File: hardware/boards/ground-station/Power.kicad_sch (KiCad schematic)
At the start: 25 parts, among them J2 Barrel_Jack, U3 TPS564242DRLR, U4 TPS564242DRLR

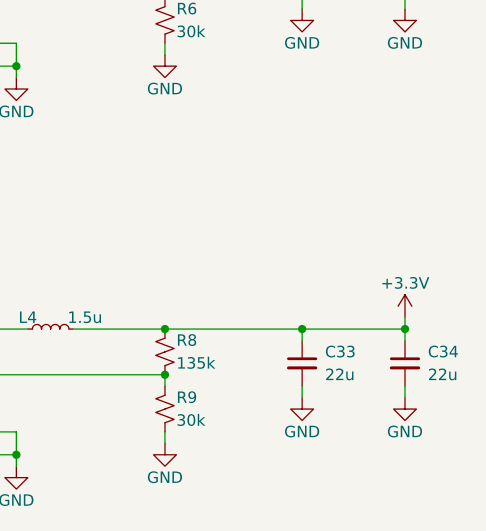
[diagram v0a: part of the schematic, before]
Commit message: Transmitting power (without wires) (wire delete)
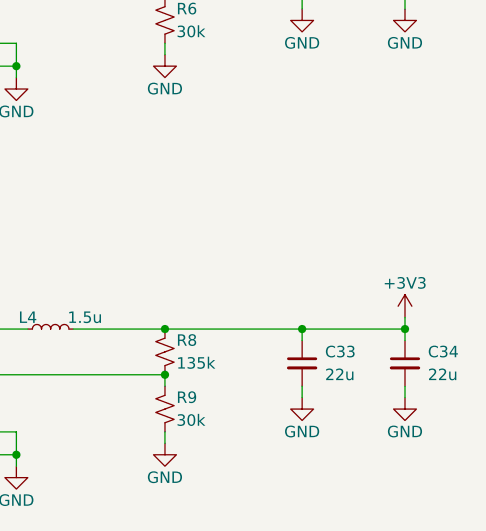
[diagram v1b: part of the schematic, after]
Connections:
- net +3.3V renamed +3V3
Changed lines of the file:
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@@
+    )
+  )
+  (symbol (lib_id "power:+3V3") (at 220.98 81.28 0) (unit 1)
+    (in_bom yes) (on_board yes) (dnp no)
+    (property "Reference" "#PWR0604" (at 220.98 85.09 0)
+      (effects (font (size 1.27 1.27)) hide)
+    )
+    (property "Value" "+3V3" (at 220.98 77.47 0)
+      (effects (font (size 1.27 1.27)))
+    )
+    (property "Footprint" "" (at 220.98 81.28 0)
+      (effects (font (size 1.27 1.27)) hide)
+    )
+    (property "Datasheet" "" (at 220.98 81.28 0)
+      (effects (font (size 1.27 1.27)) hide)
+    )
+    (pin "1")
+    (instances
+      (project "ground-station"
+        (path "/ce329892-de08-4d39-b253-15f3aaf1c085/448ef7a9-bc5a-4b03-856d-4da8b62bdbd1"
+          (reference "#PWR0604") (unit 1)
+        )
+      )
     )
   )
@@
         )
       )
-    )
-  )
-  (symbol (lib_id "power:+3.3V") (at 220.98 81.28 0) (unit 1)
-    (in_bom yes) (on_board yes) (dnp no)
-    (property "Reference" "#PWR030" (at 220.98 85.09 0)
-      (effects (font (size 1.27 1.27)) hide)
-    )
-    (property "Value" "+3.3V" (at 220.98 77.47 0)
-      (effects (font (size 1.27 1.27)))
-    )
-    (property "Footprint" "" (at 220.98 81.28 0)
-      (effects (font (size 1.27 1.27)) hide)
-    )
-    (property "Datasheet" "" (at 220.98 81.28 0)
-      (effects (font (size 1.27 1.27)) hide)
-    )
-    (pin "1")
-    (instances
-      (project "ground-station"
-        (path "/ce329892-de08-4d39-b253-15f3aaf1c085/448ef7a9-bc5a-4b03-856d-4da8b62bdbd1"
-          (reference "#PWR030") (unit 1)
-        )
-      )

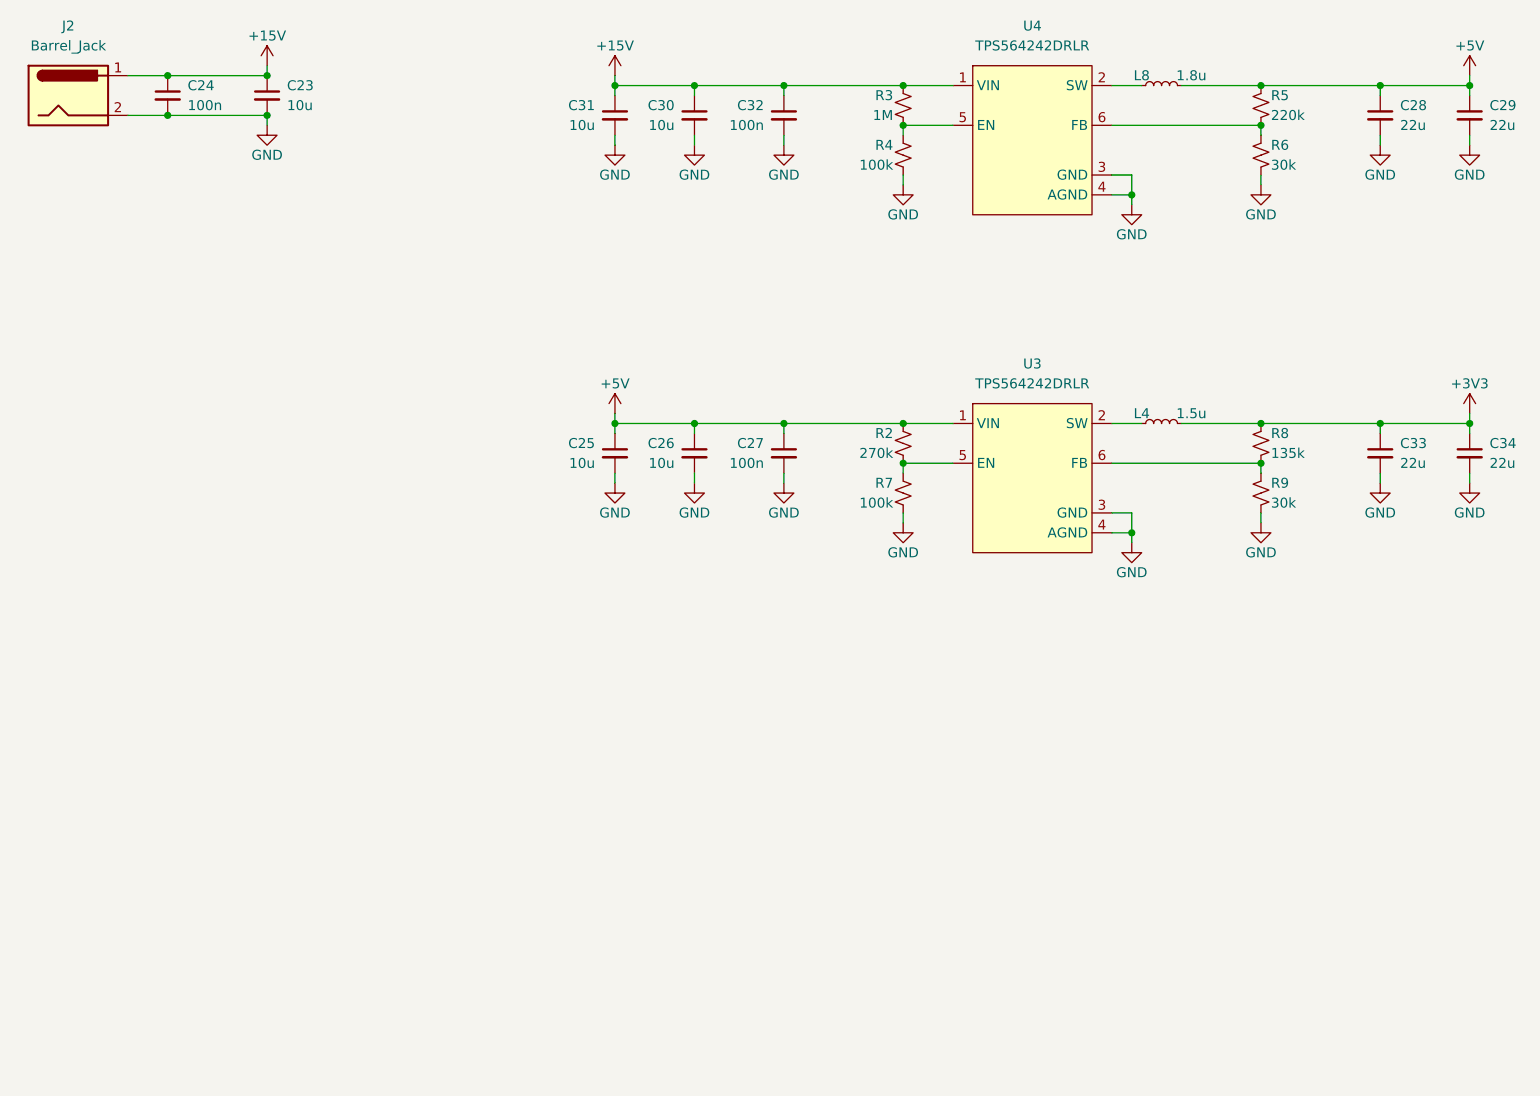
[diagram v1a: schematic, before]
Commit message: Change board input power to 5V, add connector for OTS wireless power TX
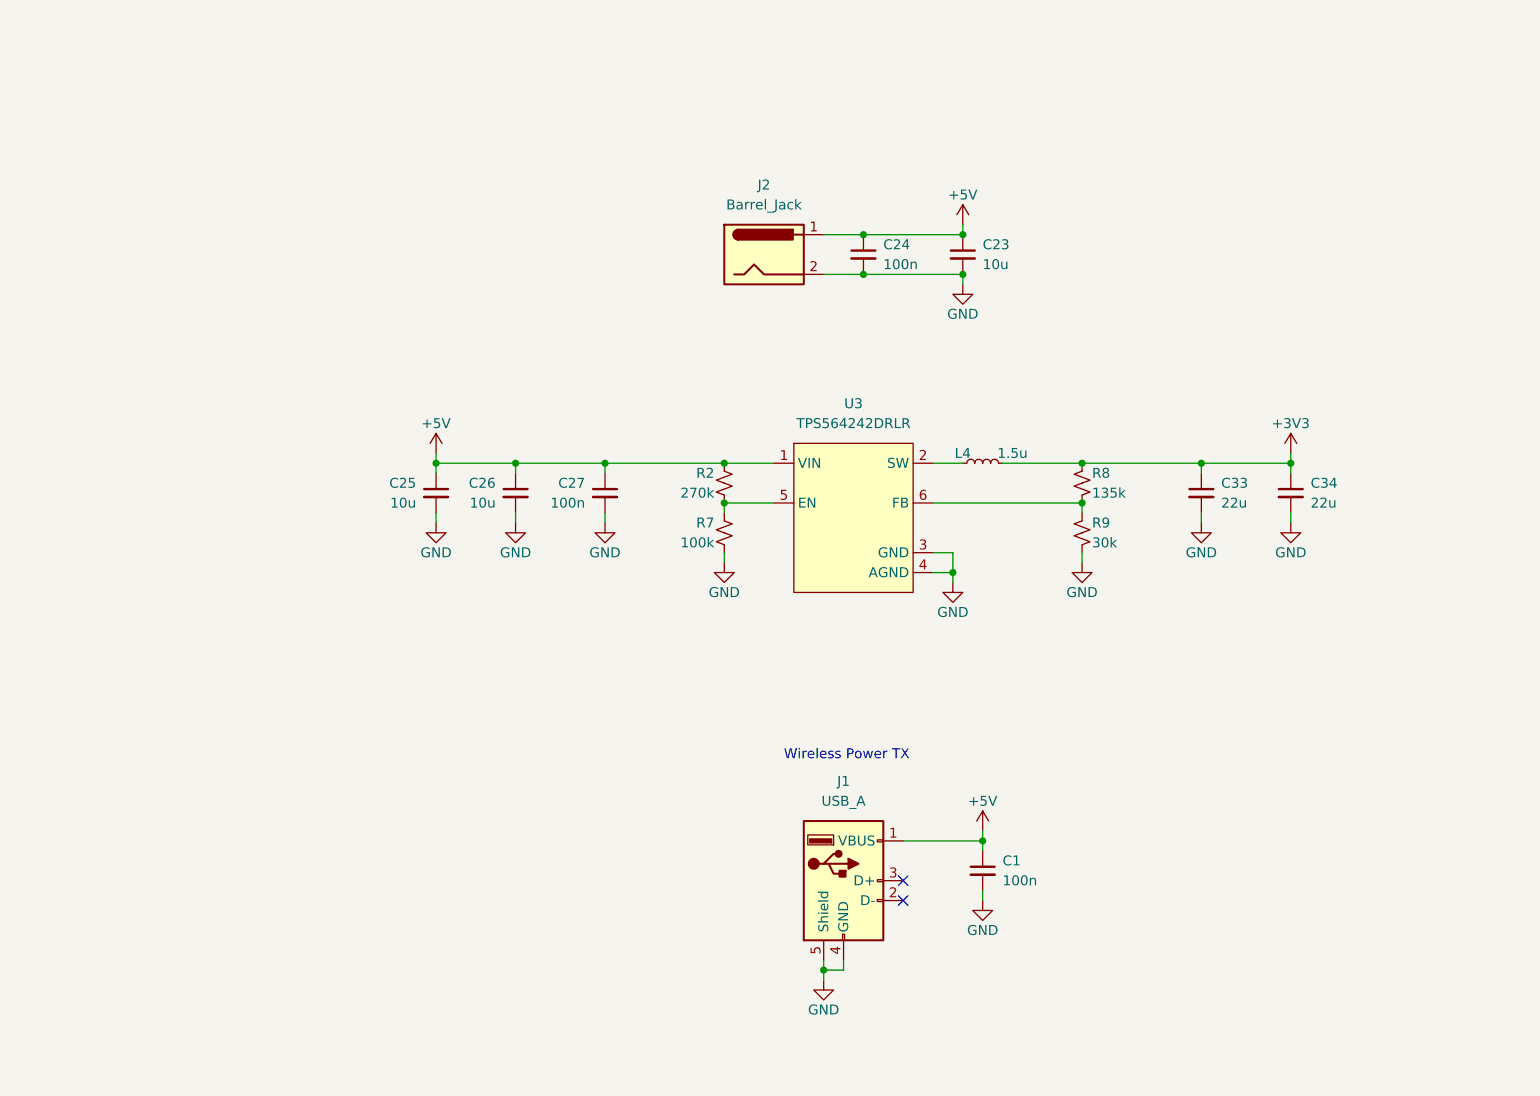
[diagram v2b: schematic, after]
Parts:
- removed C28, C29: 22u, symbol Device:C_Small
- removed C30, C31: 10u, symbol Device:C_Small
- removed C32: 100n, symbol Device:C_Small
- removed L8: 1.8u, symbol Device:L_Small
- removed R3: 1M, symbol Device:R_Small_US
- removed R4: 100k, symbol Device:R_Small_US
- removed R5: 220k, symbol Device:R_Small_US
- removed R6: 30k, symbol Device:R_Small_US
- removed U4: TPS564242DRLR, Package_TO_SOT_SMD:SOT-563, symbol capstone:TPS564242DRLR
- added C1: 100n, symbol Device:C_Small
- added J1: USB_A, symbol Connector:USB_A
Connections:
- net +15V is gone; now on net +5V: C23.1, C24.1, J2.1
- net +5V: now also C1.1, J1.1 (VBUS)
- net GND: now also C1.2, J1.4 (GND), J1.5 (Shield)
- no-connect marks 0 -> 2
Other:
- note added: "Wireless Power TX"
- moved on the sheet: C23, C24, C25, C26, C27, C33, C34, J2, L4, R2, R7, R8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

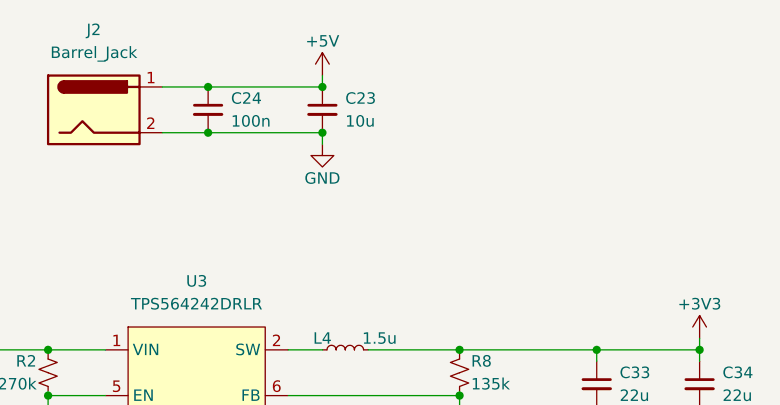
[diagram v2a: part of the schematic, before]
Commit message: Add TVS diode on 5V rail
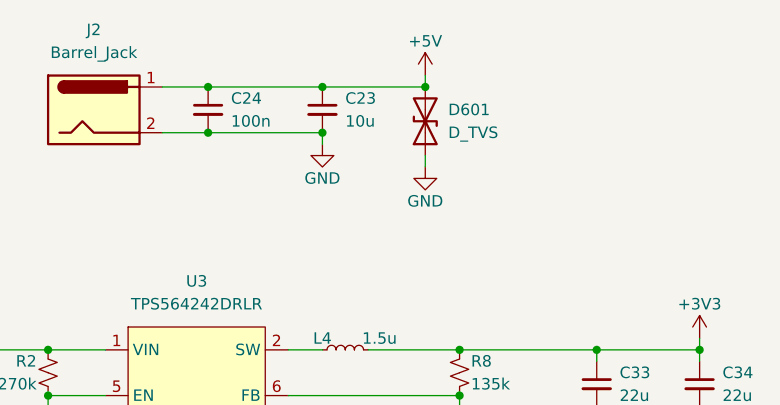
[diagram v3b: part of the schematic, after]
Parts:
- added D601: D_TVS, symbol Device:D_TVS
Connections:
- net +5V: now also D601.2 (A2)
- net GND: now also D601.1 (A1)
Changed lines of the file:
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@@
   (junction (at 143.51 63.5) (diameter 0) (color 0 0 0 0)
+  )
+  (junction (at 167.64 58.42) (diameter 0) (color 0 0 0 0)
   )
   (junction (at 171.45 87.63) (diameter 0) (color 0 0 0 0)
@@
     (stroke (width 0) (type default))
   )
-  (wire (pts (xy 156.21 58.42) (xy 156.21 57.15))
+  (wire (pts (xy 167.64 58.42) (xy 167.64 57.15))
     (stroke (width 0) (type default))
   )
@@
     (stroke (width 0) (type default))
   )
+  (wire (pts (xy 156.21 64.77) (xy 156.21 63.5))
+    (stroke (width 0) (type default))
+  )
   (wire (pts (xy 186.69 87.63) (xy 186.69 88.9))
     (stroke (width 0) (type default))
@@
     (stroke (width 0) (type default))
   )
-  (wire (pts (xy 156.21 63.5) (xy 156.21 64.77))
+  (wire (pts (xy 167.64 66.04) (xy 167.64 67.31))
+    (stroke (width 0) (type default))
+  )
+  (wire (pts (xy 167.64 58.42) (xy 156.21 58.42))
     (stroke (width 0) (type default))
   )
@@
     (effects (font (size 1.27 1.27)) (justify left bottom))
   )
-  (symbol (lib_id "power:GND") (at 156.21 64.77 0) (unit 1)
-    (in_bom yes) (on_board yes) (dnp no)
-    (property "Reference" "#PWR011" (at 156.21 71.12 0)
-      (effects (font (size 1.27 1.27)) hide)
-    )
-    (property "Value" "GND" (at 156.21 68.58 0)
-      (effects (font (size 1.27 1.27)))
-    )
-    (property "Footprint" "" (at 156.21 64.77 0)
-      (effects (font (size 1.27 1.27)) hide)
-    )
-    (property "Datasheet" "" (at 156.21 64.77 0)
+  (symbol (lib_id "power:GND") (at 167.64 67.31 0) (unit 1)
+    (in_bom yes) (on_board yes) (dnp no)
+    (property "Reference" "#PWR011" (at 167.64 73.66 0)
+      (effects (font (size 1.27 1.27)) hide)
+    )
+    (property "Value" "GND" (at 167.64 71.12 0)
+      (effects (font (size 1.27 1.27)))
+    )
+    (property "Footprint" "" (at 167.64 67.31 0)
+      (effects (font (size 1.27 1.27)) hide)
+    )
+    (property "Datasheet" "" (at 167.64 67.31 0)
       (effects (font (size 1.27 1.27)) hide)
     )
@@
       (effects (font (size 1.27 1.27)) hide)
     )
-    (pin "2")
-    (pin "1")
+    (pin "1")
+    (pin "2")
     (instances
       (project "ground-station"
@@
       (effects (font (size 1.27 1.27)) hide)
     )
-    (property "Datasheet" "" (at 142.24 87.63 0)
+    (property "Datasheet" "https://www.ti.com/lit/ds/symlink/tps564242.pdf?ts=1704720987412&ref_url=https%253A%252F%252Fwww.google.com%252F" (at 142.24 87.63 0)
       (effects (font (size 1.27 1.27)) hide)
     )
@@
       (effects (font (size 1.27 1.27)) hide)
     )
+    (pin "1")
+    (pin "2")
+    (pin "3")
     (pin "4")
-    (pin "2")
-    (pin "3")
-    (pin "1")
     (pin "5")
     (instances
@@
         (path "/ce329892-de08-4d39-b253-15f3aaf1c085/448ef7a9-bc5a-4b03-856d-4da8b62bdbd1"
           (reference "R7") (unit 1)
+        )
+      )
+    )
+  )
+  (symbol (lib_id "power:GND") (at 156.21 64.77 0) (unit 1)
+    (in_bom yes) (on_board yes) (dnp no)
+    (property "Reference" "#PWR0624" (at 156.21 71.12 0)
+      (effects (font (size 1.27 1.27)) hide)
+    )
+    (property "Value" "GND" (at 156.21 68.58 0)
+      (effects (font (size 1.27 1.27)))
+    )
+    (property "Footprint" "" (at 156.21 64.77 0)
+      (effects (font (size 1.27 1.27)) hide)
+    )
+    (property "Datasheet" "" (at 156.21 64.77 0)
+      (effects (font (size 1.27 1.27)) hide)
+    )
+    (pin "1")
+    (instances
+      (project "ground-station"
+        (path "/ce329892-de08-4d39-b253-15f3aaf1c085/448ef7a9-bc5a-4b03-856d-4da8b62bdbd1"
+          (reference "#PWR0624") (unit 1)
         )
       )
@@
     )
   )
-  (symbol (lib_id "power:+5V") (at 156.21 57.15 0) (unit 1)
-    (in_bom yes) (on_board yes) (dnp no)
-    (property "Reference" "#PWR01" (at 156.21 60.96 0)
-      (effects (font (size 1.27 1.27)) hide)
-    )
-    (property "Value" "+5V" (at 156.21 53.34 0)
-      (effects (font (size 1.27 1.27)))
-    )
-    (property "Footprint" "" (at 156.21 57.15 0)
-      (effects (font (size 1.27 1.27)) hide)
-    )
-    (property "Datasheet" "" (at 156.21 57.15 0)
+  (symbol (lib_id "power:+5V") (at 167.64 57.15 0) (unit 1)
+    (in_bom yes) (on_board yes) (dnp no)
+    (property "Reference" "#PWR01" (at 167.64 60.96 0)
+      (effects (font (size 1.27 1.27)) hide)
+    )
+    (property "Value" "+5V" (at 167.64 53.34 0)
+      (effects (font (size 1.27 1.27)))
+    )
+    (property "Footprint" "" (at 167.64 57.15 0)
+      (effects (font (size 1.27 1.27)) hide)
+    )
+    (property "Datasheet" "" (at 167.64 57.15 0)
       (effects (font (size 1.27 1.27)) hide)
     )
@@
         )
       )
+    )
+  )
+  (symbol (lib_id "Device:D_TVS") (at 167.64 62.23 90) (unit 1)
+    (in_bom yes) (on_board yes) (dnp no) (fields_autoplaced)
+    (property "Reference" "D601" (at 170.18 60.96 90)
+      (effects (font (size 1.27 1.27)) (justify right))
+    )
+    (property "Value" "D_TVS" (at 170.18 63.5 90)
+      (effects (font (size 1.27 1.27)) (justify right))
+    )
+    (property "Footprint" "" (at 167.64 62.23 0)
+      (effects (font (size 1.27 1.27)) hide)
+    )
+    (property "Datasheet" "~" (at 167.64 62.23 0)
+      (effects (font (size 1.27 1.27)) hide)
+    )
+    (pin "1")
+    (pin "2")
+    (instances
+      (project "ground-station"
+        (path "/ce329892-de08-4d39-b253-15f3aaf1c085/448ef7a9-bc5a-4b03-856d-4da8b62bdbd1"
+          (reference "D601") (unit 1)
+        )
+      )

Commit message: sch review
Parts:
- added C2: ~, symbol Device:C_Small
- added R1: 0, symbol Device:R_Small_US
- R2: value 270k -> 0
- R7: now not fitted
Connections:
- net +3V3: now also C2.2
- net GND: now also R1.2; no longer J1.5 (Shield)
- net at R8.2, R9.1, U3.6 (FB): now also C2.1
- new net: J1.5 (Shield), R1.1
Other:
- moved on the sheet: C33, C34

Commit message: Added footprints for most things
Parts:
- C1, C24, C27: footprint (none) -> Capacitor_SMD:C_0201_0603Metric
- C2, C23, C25, C26: footprint (none) -> Capacitor_SMD:C_0603_1608Metric
- C33, C34: footprint (none) -> Capacitor_SMD:C_0805_2012Metric
- J1: Part No (none) -> USB-A-S-RA
- L4: footprint (none) -> capstone:FNR6028S1R5MT
- R1, R2, R7: footprint (none) -> Resistor_SMD:R_0402_1005Metric
- R8: footprint (none) -> Resistor_SMD:R_0603_1608Metric
- R9: footprint (none) -> Resistor_SMD:R_0201_0603Metric
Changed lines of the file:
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@@
       (effects (font (size 1.27 1.27)) (justify left))
     )
-    (property "Footprint" "" (at 220.98 91.44 0)
+    (property "Footprint" "Capacitor_SMD:C_0805_2012Metric" (at 220.98 91.44 0)
       (effects (font (size 1.27 1.27)) hide)
     )
@@
       (effects (font (size 1.27 1.27)) (justify right))
     )
-    (property "Footprint" "" (at 171.45 96.52 0)
+    (property "Footprint" "Resistor_SMD:R_0201_0603Metric" (at 171.45 96.52 0)
       (effects (font (size 1.27 1.27)) hide)
     )
@@
       (effects (font (size 1.27 1.27)) (justify right))
     )
-    (property "Footprint" "" (at 185.42 90.17 0)
+    (property "Footprint" "Capacitor_SMD:C_0603_1608Metric" (at 185.42 90.17 0)
       (effects (font (size 1.27 1.27)) hide)
     )
@@
       (effects (font (size 1.27 1.27)) hide)
     )
-    (pin "2")
-    (pin "1")
+    (pin "1")
+    (pin "2")
     (instances
       (project "ground-station"
@@
       (effects (font (size 1.27 1.27)) (justify left))
     )
-    (property "Footprint" "" (at 209.55 91.44 0)
+    (property "Footprint" "Capacitor_SMD:C_0805_2012Metric" (at 209.55 91.44 0)
       (effects (font (size 1.27 1.27)) hide)
     )
@@
       (effects (font (size 1.27 1.27)))
     )
-    (property "Footprint" "" (at 158.75 87.63 0)
+    (property "Footprint" "capstone:FNR6028S1R5MT" (at 158.75 87.63 0)
       (effects (font (size 1.27 1.27)) hide)
     )
@@
       (effects (font (size 1.27 1.27)) (justify left))
     )
-    (property "Footprint" "" (at 158.75 139.7 0)
+    (property "Footprint" "Capacitor_SMD:C_0201_0603Metric" (at 158.75 139.7 0)
       (effects (font (size 1.27 1.27)) hide)
     )
@@
       (effects (font (size 1.27 1.27)) (justify right))
     )
-    (property "Footprint" "" (at 88.9 91.44 0)
+    (property "Footprint" "Capacitor_SMD:C_0603_1608Metric" (at 88.9 91.44 0)
       (effects (font (size 1.27 1.27)) hide)
     )
@@
       (effects (font (size 1.27 1.27)) (justify left))
     )
-    (property "Footprint" "" (at 138.43 156.21 0)
+    (property "Footprint" "Resistor_SMD:R_0402_1005Metric" (at 138.43 156.21 0)
       (effects (font (size 1.27 1.27)) hide)
     )
@@
       (effects (font (size 1.27 1.27)) hide)
     )
-    (pin "2")
-    (pin "1")
+    (pin "1")
+    (pin "2")
     (instances
       (project "ground-station"
@@
       (effects (font (size 1.27 1.27)) (justify right))
     )
-    (property "Footprint" "" (at 125.73 90.17 0)
+    (property "Footprint" "Resistor_SMD:R_0402_1005Metric" (at 125.73 90.17 0)
       (effects (font (size 1.27 1.27)) hide)
     )
@@
       (effects (font (size 1.27 1.27)) (justify right))
     )
-    (property "Footprint" "" (at 99.06 91.44 0)
+    (property "Footprint" "Capacitor_SMD:C_0603_1608Metric" (at 99.06 91.44 0)
       (effects (font (size 1.27 1.27)) hide)
     )
@@
       (effects (font (size 1.27 1.27)) hide)
     )
-    (property "Datasheet" " ~" (at 144.78 142.24 0)
+    (property "Datasheet" "https://app.adam-tech.com/products/download/data_sheet/195865/usb-a-s-ra-data-sheet.pdf" (at 144.78 142.24 0)
+      (effects (font (size 1.27 1.27)) hide)
+    )
+    (property "Part No" "USB-A-S-RA" (at 140.97 140.97 0)
       (effects (font (size 1.27 1.27)) hide)
     )
@@
       (effects (font (size 1.27 1.27)) (justify right))
     )
-    (property "Footprint" "" (at 110.49 91.44 0)
+    (property "Footprint" "Capacitor_SMD:C_0201_0603Metric" (at 110.49 91.44 0)
       (effects (font (size 1.27 1.27)) hide)
     )
@@
       (effects (font (size 1.27 1.27)) (justify right))
     )
-    (property "Footprint" "" (at 171.45 90.17 0)
+    (property "Footprint" "Resistor_SMD:R_0603_1608Metric" (at 171.45 90.17 0)
       (effects (font (size 1.27 1.27)) hide)
     )
@@
       (effects (font (size 1.27 1.27)) (justify right))
     )
-    (property "Footprint" "" (at 125.73 96.52 0)
+    (property "Footprint" "Resistor_SMD:R_0402_1005Metric" (at 125.73 96.52 0)
       (effects (font (size 1.27 1.27)) hide)
     )
@@
       (effects (font (size 1.27 1.27)) (justify left))
     )
-    (property "Footprint" "" (at 156.21 60.96 0)
+    (property "Footprint" "Capacitor_SMD:C_0603_1608Metric" (at 156.21 60.96 0)
       (effects (font (size 1.27 1.27)) hide)
     )
@@
       (effects (font (size 1.27 1.27)) (justify left))
     )
-    (property "Footprint" "" (at 143.51 60.96 0)
-      (effects (font (size 1.27 1.27)) hide)
-    )
+    (property "Footprint" "Capacitor_SMD:C_0201_0603Metric" (at 143.51 60.96 0)
+      (effects (font (size 1.27 1.27)) hide)
+    )
